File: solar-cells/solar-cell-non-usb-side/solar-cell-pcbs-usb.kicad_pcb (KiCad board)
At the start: 2 copper layers, 80 x 103.5 mm, 22 parts, among them J1 Solar Cell

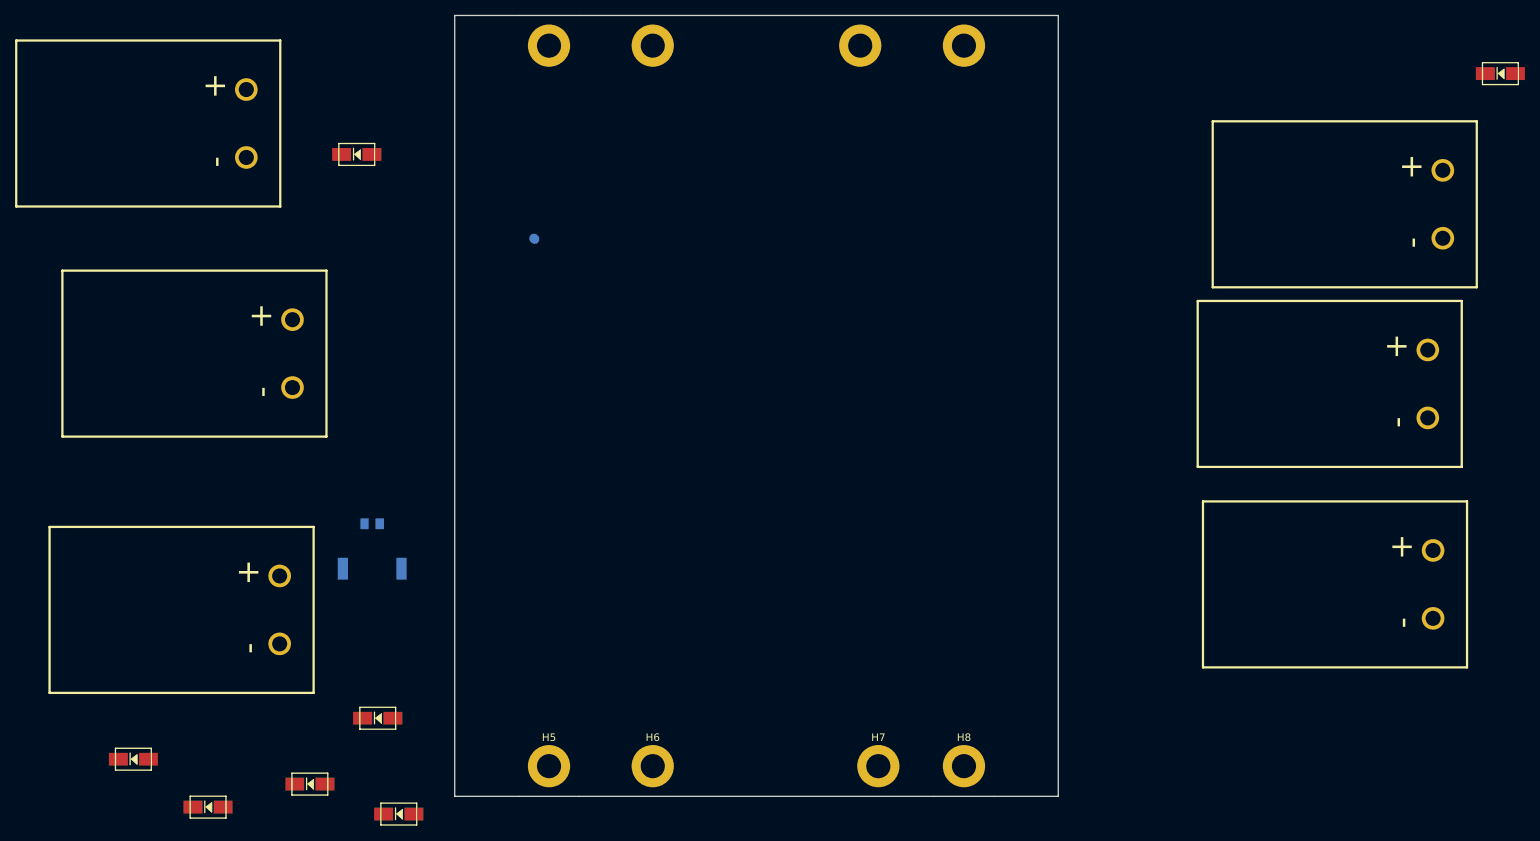
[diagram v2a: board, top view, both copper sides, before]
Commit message: solar cell pcb laid out
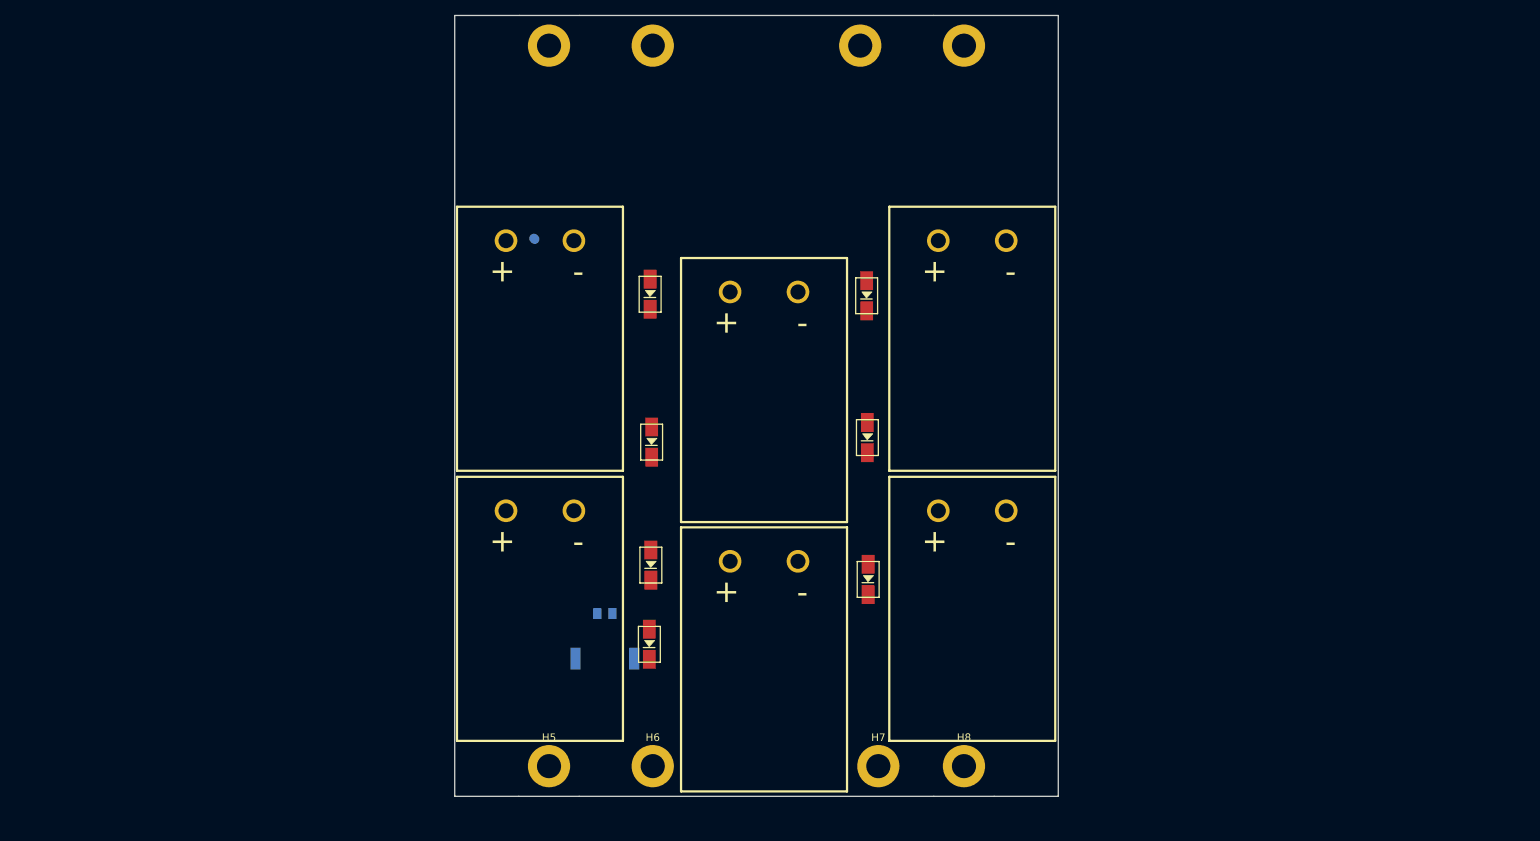
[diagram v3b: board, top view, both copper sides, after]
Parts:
- moved SC4 118.7 mm to (83.9, 117.4), turned to 90 degrees
- moved D3 115.0 mm to (126.7, 75.9), turned to 90 degrees
- moved SC5 108.3 mm to (113.6, 124.1), turned to 90 degrees
- moved D4 96.8 mm to (126.8, 94.7), turned to 90 degrees
- moved D1 79.1 mm to (98.0, 75.7), turned to 90 degrees
- moved D2 76.1 mm to (98.2, 95.3), turned to 90 degrees
- moved SC2 76.1 mm to (113.6, 88.4), turned to 90 degrees
- moved D9 75.6 mm to (97.9, 122.1), turned to 90 degrees
- moved D6 69.6 mm to (126.9, 113.5), turned to 90 degrees
- moved SC1 60.3 mm to (83.9, 81.6), turned to 90 degrees
- moved SC3 57.9 mm to (141.2, 81.6), turned to 90 degrees
- moved SC6 55.3 mm to (141.2, 117.4), turned to 90 degrees
- moved D5 41.5 mm to (98.1, 111.6), turned to 90 degrees
- moved J1 33.1 mm to (93.0, 118.0)

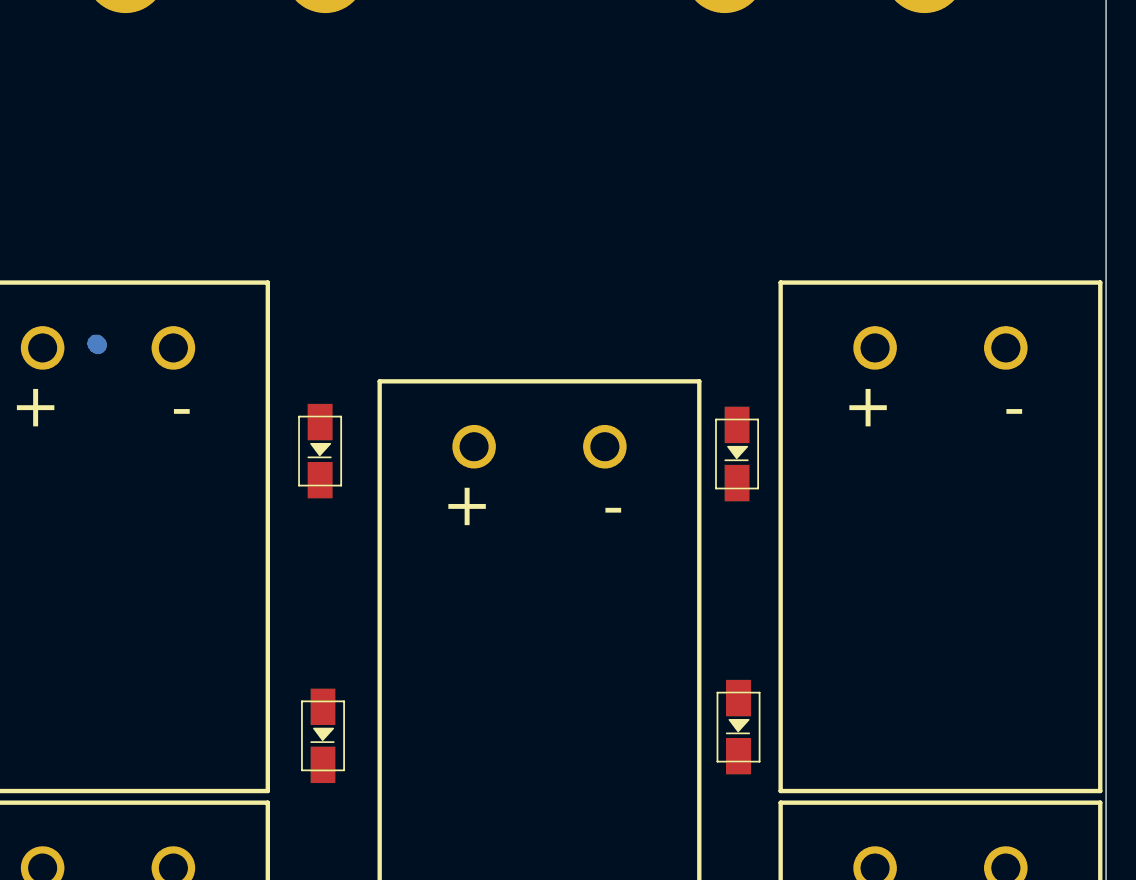
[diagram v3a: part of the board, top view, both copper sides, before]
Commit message: added usbc hole
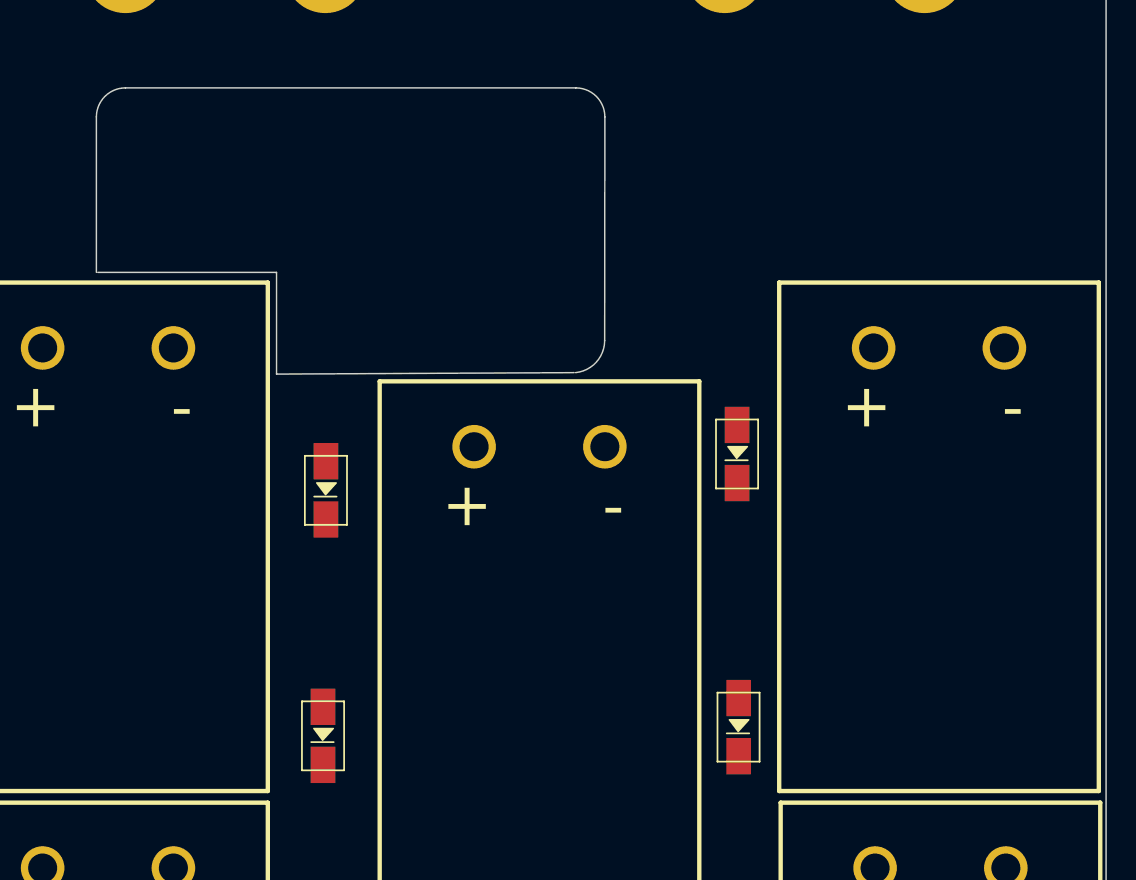
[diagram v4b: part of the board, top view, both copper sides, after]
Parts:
- moved D1 2.73 mm to (98.4, 78.4)
- moved SC3 0.10 mm to (141.1, 81.6)
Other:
- outline, holes or cut-outs redrawn
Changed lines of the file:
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@@
   )
   (footprint "ISP:SM101K07TF" (layer "F.Cu")
-    (at 141.2 81.6 90)
+    (at 141.1 81.6 90)
     (property "Sheetfile" "solar-cell-pcbs-usb.kicad_sch")
     (property "Sheetname" "")
@@
   )
   (footprint "ISP:DO-214AC" (layer "F.Cu")
-    (at 98 75.7 90)
+    (at 98.4 78.4 90)
     (property "Sheetfile" "solar-cell-pcbs-usb.kicad_sch")
     (property "Sheetname" "")
@@
   )
   (gr_line (start 143.6 38.75) (end 152.1 38.75) (layer "Edge.Cuts") (width 0.1))
+  (gr_line (start 95 70.4) (end 95 63.4) (layer "Edge.Cuts") (width 0.1))
   (gr_line (start 80.6 142.25) (end 88.6 142.25) (layer "Edge.Cuts") (width 0.1))
   (gr_line (start 135.6 142.25) (end 88.6 142.25) (layer "Edge.Cuts") (width 0.1))
@@
   (gr_line (start 152.1 38.75) (end 152.1 142.25) (layer "Edge.Cuts") (width 0.1))
   (gr_line (start 80.6 142.25) (end 72.1 142.25) (layer "Edge.Cuts") (width 0.1))
+  (gr_line (start 82.6 63.4) (end 82.6 52.7) (layer "Edge.Cuts") (width 0.1))
   (gr_line (start 143.6 142.25) (end 152.1 142.25) (layer "Edge.Cuts") (width 0.1))
+  (gr_line (start 95 70.4) (end 115.485786 70.3) (layer "Edge.Cuts") (width 0.1))
+  (gr_arc (start 117.585786 68.085786) (mid 117.011763 69.577659) (end 115.585786 70.3) (layer "Edge.Cuts") (width 0.1))
+  (gr_arc (start 115.599999 50.700001) (mid 117.014213 51.285787) (end 117.599999 52.700001) (layer "Edge.Cuts") (width 0.1))
+  (gr_arc (start 82.6 52.7) (mid 83.185786 51.285786) (end 84.6 50.7) (layer "Edge.Cuts") (width 0.1))
   (gr_line (start 135.6 142.25) (end 143.6 142.25) (layer "Edge.Cuts") (width 0.1))
+  (gr_line (start 117.6 52.7) (end 117.585786 68.085786) (layer "Edge.Cuts") (width 0.1))
   (gr_line (start 88.65 38.75) (end 135.6 38.75) (layer "Edge.Cuts") (width 0.1))
+  (gr_line (start 84.6 50.7) (end 115.6 50.7) (layer "Edge.Cuts") (width 0.1))
   (gr_line (start 80.65 38.75) (end 72.1 38.75) (layer "Edge.Cuts") (width 0.1))
   (gr_line (start 72.1 142.25) (end 72.1 38.75) (layer "Edge.Cuts") (width 0.1))
+  (gr_line (start 95 63.4) (end 82.7 63.4) (layer "Edge.Cuts") (width 0.1))
   (dimension (type aligned) (layer "Dwgs.User")
     (pts (xy 98.35 138.25) (xy 98.25 124.025))
@@
     (style (thickness 0.15) (arrow_length 1.27) (text_position_mode 0) (extension_height 0.58642) (extension_offset 0.5) keep_text_aligned)
   )
-  (segment (start 82.6 68.3) (end 82.7 68.4) (width 1.27) (layer "B.Cu") (net 3))
 )
